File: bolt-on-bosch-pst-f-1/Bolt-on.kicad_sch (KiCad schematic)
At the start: 10 parts

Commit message: update readme
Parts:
- removed JPST-F_1_IN1: Conn_01x04, Connector_JST:JST_PH_S4B-PH-K_1x04_P2.00mm_Horizontal, symbol Connector_Generic:Conn_01x04
- added PST-F1_IN1: Conn_01x04, Connector_JST:JST_PH_S4B-PH-K_1x04_P2.00mm_Horizontal, symbol Connector_Generic:Conn_01x04
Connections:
- net +5V: now also PST-F1_IN1.1 (5V)
- net GND: now also PST-F1_IN1.4 (GND)
- net IO35: now also D1.1; no longer D1.2
- net IO36: now also D1.2, PST-F1_IN1.3 (TEMP_SIG)
- net at R_PRESS_TOP1.2: now also PST-F1_IN1.2 (PRESS_SIG)
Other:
- moved on the sheet: D1

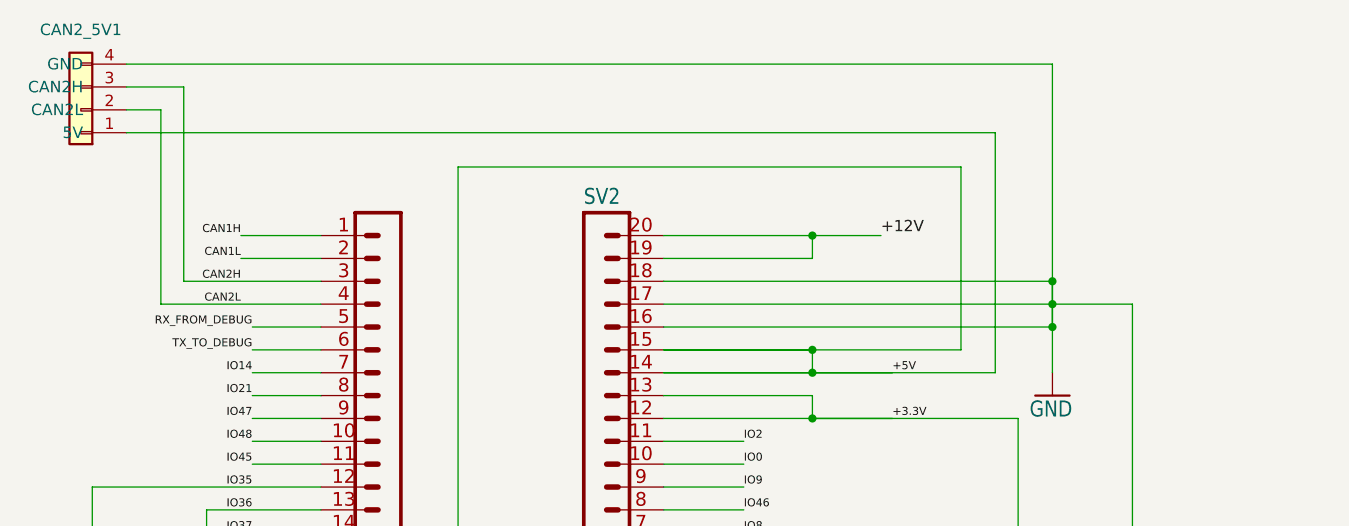
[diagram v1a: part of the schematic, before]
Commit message: add copper pour to gnd and 5v
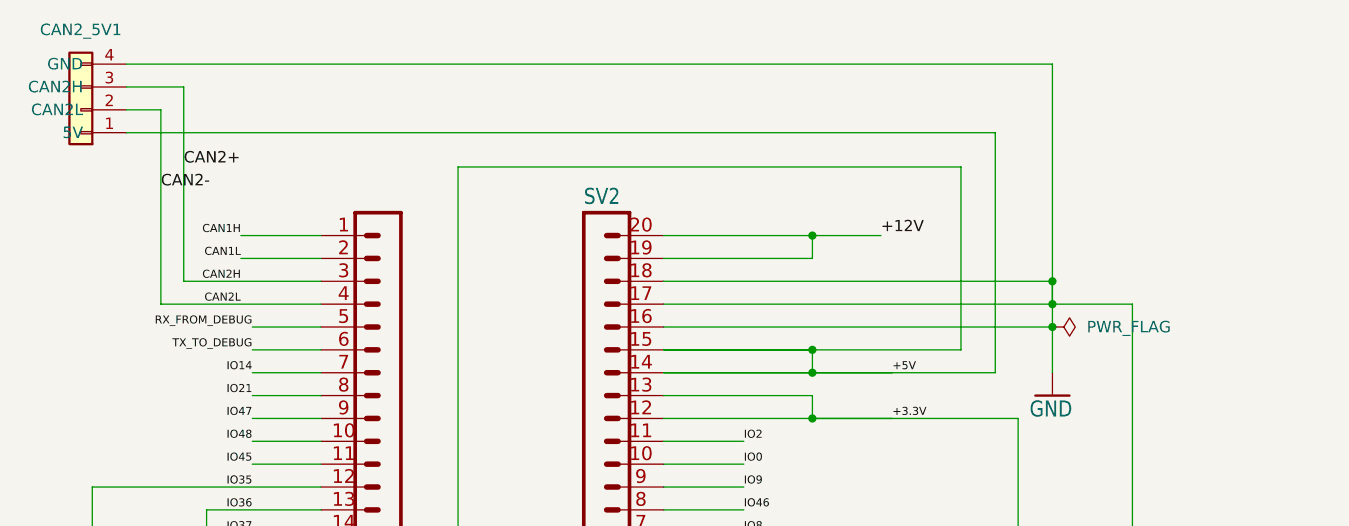
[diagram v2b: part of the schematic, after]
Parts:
- CAN2_5V1, PST-F1_IN1: footprint Connector_JST:JST_PH_S4B-PH-K_1x04_P2.00mm_Horizontal -> Connector_JST:JST_PH_S4B-PH-SM4-TB_1x04-1MP_P2.00mm_Horizontal
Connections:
- net CAN2H renamed CAN2+
- net CAN2L renamed CAN2-
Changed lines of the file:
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@@
+	)
+	(junction
+		(at 274.32 135.89)
+		(diameter 0)
+		(color 0 0 0 0)
 	)
 	(junction
@@
 	)
 	(junction
-		(at 274.32 135.89)
-		(diameter 0)
-		(color 0 0 0 0)
-	)
-	(junction
 		(at 208.28 219.71)
 		(diameter 0)
@@
 	(wire
 		(pts
+			(xy 274.32 135.89) (xy 274.32 140.97)
+		)
+		(stroke
+			(width 0)
+			(type default)
+		)
+	)
+	(wire
+		(pts
 			(xy 193.04 171.45) (xy 185.42 171.45)
 		)
@@
 		(pts
 			(xy 274.32 106.68) (xy 274.32 130.81)
-		)
-		(stroke
-			(width 0)
-			(type default)
-		)
-	)
-	(wire
-		(pts
-			(xy 274.32 135.89) (xy 274.32 140.97)
-		)
-		(stroke
-			(width 0.1524)
-			(type solid)
-		)
-	)
-	(wire
-		(pts
-			(xy 274.32 133.35) (xy 274.32 135.89)
 		)
 		(stroke
@@
 		)
 	)
+	(label "CAN2-"
+		(at 175.26 120.65 0)
+		(fields_autoplaced yes)
+		(effects
+			(font
+				(size 1.27 1.27)
+			)
+			(justify left bottom)
+		)
+		(property "Netclass" "Default"
+			(at 175.26 121.92 0)
+			(effects
+				(font
+					(size 1.27 1.27)
+					(italic yes)
+				)
+				(justify left)
+				(hide yes)
+			)
+		)
+	)
 	(label "IO5"
 		(at 240.03 171.45 0)
@@
 			)
 			(justify left bottom)
+		)
+	)
+	(label "CAN2+"
+		(at 177.8 118.11 0)
+		(fields_autoplaced yes)
+		(effects
+			(font
+				(size 1.27 1.27)
+			)
+			(justify left bottom)
+		)
+		(property "Netclass" "Default"
+			(at 177.8 119.38 0)
+			(effects
+				(font
+					(size 1.27 1.27)
+					(italic yes)
+				)
+				(justify left)
+				(hide yes)
+			)
 		)
 	)
@@
 				(path "/d642a88c-4bf2-433d-8cf9-b5aeaa3805cb"
 					(reference "C1")
+					(unit 1)
+				)
+			)
+		)
+	)
+	(symbol
+		(lib_id "power:PWR_FLAG")
+		(at 274.32 135.89 270)
+		(unit 1)
+		(exclude_from_sim no)
+		(in_bom yes)
+		(on_board yes)
+		(dnp no)
+		(fields_autoplaced yes)
+		(property "Reference" "#FLG01"
+			(at 276.225 135.89 0)
+			(effects
+				(font
+					(size 1.27 1.27)
+				)
+				(hide yes)
+			)
+		)
+		(property "Value" "PWR_FLAG"
+			(at 278.13 135.8899 90)
+			(effects
+				(font
+					(size 1.27 1.27)
+				)
+				(justify left)
+			)
+		)
+		(property "Footprint" ""
+			(at 274.32 135.89 0)
+			(effects
+				(font
+					(size 1.27 1.27)
+				)
+				(hide yes)
+			)
+		)
+		(property "Datasheet" "~"
+			(at 274.32 135.89 0)
+			(effects
+				(font
+					(size 1.27 1.27)
+				)
+				(hide yes)
+			)
+		)
+		(property "Description" "Special symbol for telling ERC where power comes from"
+			(at 274.32 135.89 0)
+			(effects
+				(font
+					(size 1.27 1.27)
+				)
+				(hide yes)
+			)
+		)
+		(pin "1"
+		)
+		(instances
+			(project ""
+				(path "/d642a88c-4bf2-433d-8cf9-b5aeaa3805cb"
+					(reference "#FLG01")
 					(unit 1)
 				)
@@
 			)
 		)
-		(property "Footprint" "Connector_JST:JST_PH_S4B-PH-K_1x04_P2.00mm_Horizontal"
+		(property "Footprint" "Connector_JST:JST_PH_S4B-PH-SM4-TB_1x04-1MP_P2.00mm_Horizontal"
 			(at 223.52 191.77 0)
 			(effects
@@
 		)
 		(property "Value" "Conn_01x04"
-			(at 166.37 102.87 0)
-			(effects
-				(font
-					(size 1.27 1.27)
-				)
-				(hide yes)
-			)
-		)
-		(property "Footprint" "Connector_JST:JST_PH_S4B-PH-K_1x04_P2.00mm_Horizontal"
-			(at 166.37 111.76 0)
+			(at 155.194 102.87 0)
+			(effects
+				(font
+					(size 1.27 1.27)
+				)
+				(hide yes)
+			)
+		)
+		(property "Footprint" "Connector_JST:JST_PH_S4B-PH-SM4-TB_1x04-1MP_P2.00mm_Horizontal"
+			(at 169.418 100.33 0)
 			(effects
 				(font
@@
 		)
 		(property "Description" "Generic connector, single row, 01x04, script generated (kicad-library-utils/schlib/autogen/connector/)"
-			(at 166.37 111.76 0)
-			(effects
-				(font
+			(at 166.624 98.044 0)
+			(effects
+				(font

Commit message: swaped jst positions
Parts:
- added C3: ﻿0.1µF, Capacitor_SMD:C_0805_2012Metric_Pad1.18x1.45mm_HandSolder, symbol Device:C
- added C4: 1µF, Capacitor_SMD:C_0805_2012Metric_Pad1.18x1.45mm_HandSolder, symbol Device:C
- added C5: 10µF, Capacitor_SMD:C_1206_3216Metric_Pad1.33x1.80mm_HandSolder, symbol Device:C
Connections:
- net +5V: now also C3.2, C4.2, C5.2
- net GND: now also C3.1, C4.1, C5.1
